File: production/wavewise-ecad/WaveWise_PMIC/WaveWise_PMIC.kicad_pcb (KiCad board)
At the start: 4 copper layers, 88.9 x 80 mm, 63 parts, among them IC1 LV14360PDDAR, J10 5031590200, J11 5031590200, J13 Screw_Terminal_01x03, J2 Conn_01x06_Pin, J3 Conn_01x03_Pin, J5 5031590400, J6 5031590400, J8 5031590800, J9 5031590300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

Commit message: Update WaveWise_PMIC.kicad_pcb
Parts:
- moved J2 1.02 mm to (59.7, 80.8)
- moved R20 0.80 mm to (52.8, 59.9)
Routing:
- net /Connectors/GPIO4: track 0.00 -> 7.37 mm
- net /Connectors/GPIO3: track 0.00 -> 7.37 mm
- net /Connectors/GPIO2: track 0.00 -> 7.37 mm
- net /Connectors/GPIO1: track 0.00 -> 7.37 mm
- net GND: track 88.3 -> 93.3 mm, vias 12 -> 14
- net Net-(H1-Pad1): track 0.00 -> 4.71 mm
- net panel_sense: track 53.7 -> 55.5 mm
- net batt_sense: track 58.6 -> 59.9 mm

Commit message: fix drc
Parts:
- moved R19 26.6 mm to (60.3, 55.2), turned to 0 degrees
- moved R16 23.5 mm to (60.3, 57.8), turned to 180 degrees
- moved HE1 1.61 mm to (54.6, 127.0)
- moved R1 1.27 mm to (111.5, 57.7)
- moved R2 1.27 mm to (109.2, 57.7)
- moved H1 1.08 mm to (54.6, 54.6)
- moved H2 1.08 mm to (135.9, 54.6)
- moved H4 0.36 mm to (135.9, 127.0)
- moved R23 0.25 mm to (135.8, 120.4)
- moved R20 0.25 mm to (52.6, 59.9)
- moved R12 0.13 mm to (60.2, 62.9)
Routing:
- net /Connectors/rockblock_TX: track 16.8 -> 44.7 mm
- net /Connectors/BICO_UART_TX: track 34.7 -> 7.54 mm
- net /Connectors/rockblock_RX: track 16.5 -> 41.7 mm
- net /Connectors/BICO_UART_RX: track 32.0 -> 7.54 mm
- net /Connectors/PANEL_SENSE_DIO: track 0.00 -> 6.00 mm
- net /Connectors/BATT_SENSE_DIO: track 0.00 -> 5.95 mm
- net /Connectors/Batt V Sense: track 92.2 -> 90.0 mm
- net +BATT: track 9.01 -> 10.5 mm
- net Net-(H1-Pad1): track 4.71 -> 5.26 mm

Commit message: power stuff
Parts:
- J5: footprint Unchecked:4pinmolex -> Connector_Molex:Molex_Micro-Fit_3.0_43650-0400_1x04_P3.00mm_Horizontal
- moved R26 21.5 mm to (91.4, 101.5), turned to 90 degrees
- moved J5 3.55 mm to (130.0, 76.1)
- moved R8 1.03 mm to (93.8, 101.3), turned to -90 degrees
- moved R25 0.40 mm to (62.9, 105.7), turned to 180 degrees
- moved R6 0.25 mm to (67.1, 113.3)
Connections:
- J13 pad 2: Net-(J13-Pin_2) -> /Inverter_Input
- J8 pad 5: air_comp_dio -> /Connectors/SICO_PUMP_CONTROL
- K1 pad 1: Net-(D2-A) -> +48V
- K1 pad 2: +48V -> Net-(D2-A)
- R25 pad 1: air_comp_dio -> /PUMP_CONTROL
- R25 pad 2: Net-(J13-Pin_2) -> /Connectors/SICO_PUMP_CONTROL
- R26 pad 1: Net-(J13-Pin_2) -> /PICO (BICO)/BICO_PUMP_CTRL
- R26 pad 2: /Inverter_Input -> /PUMP_CONTROL
- R8 pad 1: /PICO (BICO)/PUMP_CTRL -> /PUMP_CONTROL
- U1 pad 7: /PICO (BICO)/PUMP_CTRL -> /PICO (BICO)/BICO_PUMP_CTRL
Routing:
- net Net-(J13-Pin_2): track 81.4 -> 0.00 mm, vias 2 -> 0
- net /PICO (BICO)/PUMP_CTRL: track 52.8 -> 0.00 mm, vias 1 -> 0
- net /PICO (BICO)/BICO_PUMP_CTRL: track 0.00 -> 26.2 mm, vias 0 -> 1
- net /Inverter_Input: track 20.7 -> 35.6 mm
- net Net-(D2-A): track 21.1 -> 11.9 mm
- net +5V: track 38.5 -> 45.6 mm
- net Net-(Q2-B): track 4.90 -> 0.00 mm
- net /BOUT2: track 11.0 -> 6.31 mm
- net air_comp_dio: track 4.45 -> 0.00 mm
- net /Connectors/SICO_PUMP_CONTROL: track 0.00 -> 4.45 mm
- net /AOUT2: track 11.7 -> 7.28 mm
- net /PUMP_CONTROL: track 0.00 -> 4.42 mm, vias 0 -> 1
- net Net-(D1-K): track 30.3 -> 26.2 mm
- net GND: track 93.6 -> 96.2 mm, vias 14 -> 13
- net /AOUT1: track 10.4 -> 8.07 mm
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
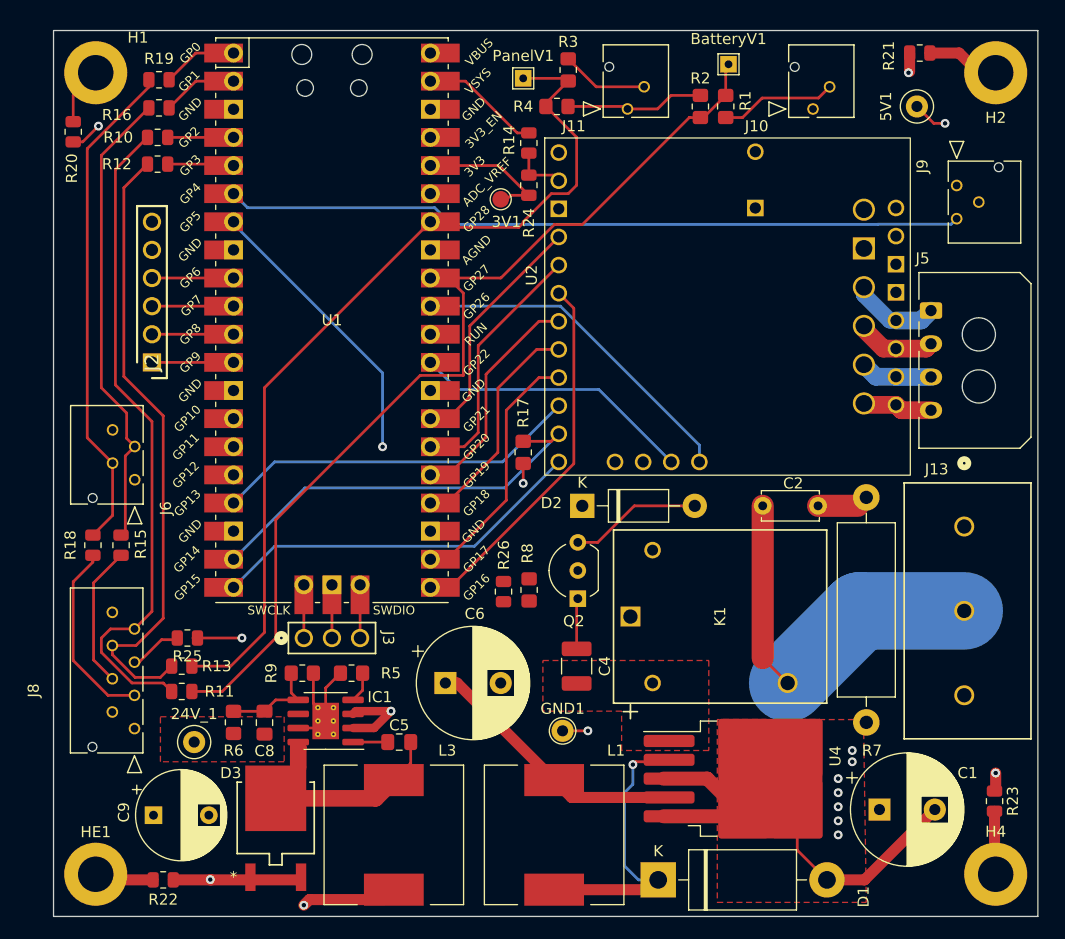
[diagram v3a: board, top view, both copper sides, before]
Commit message: add silkscreen
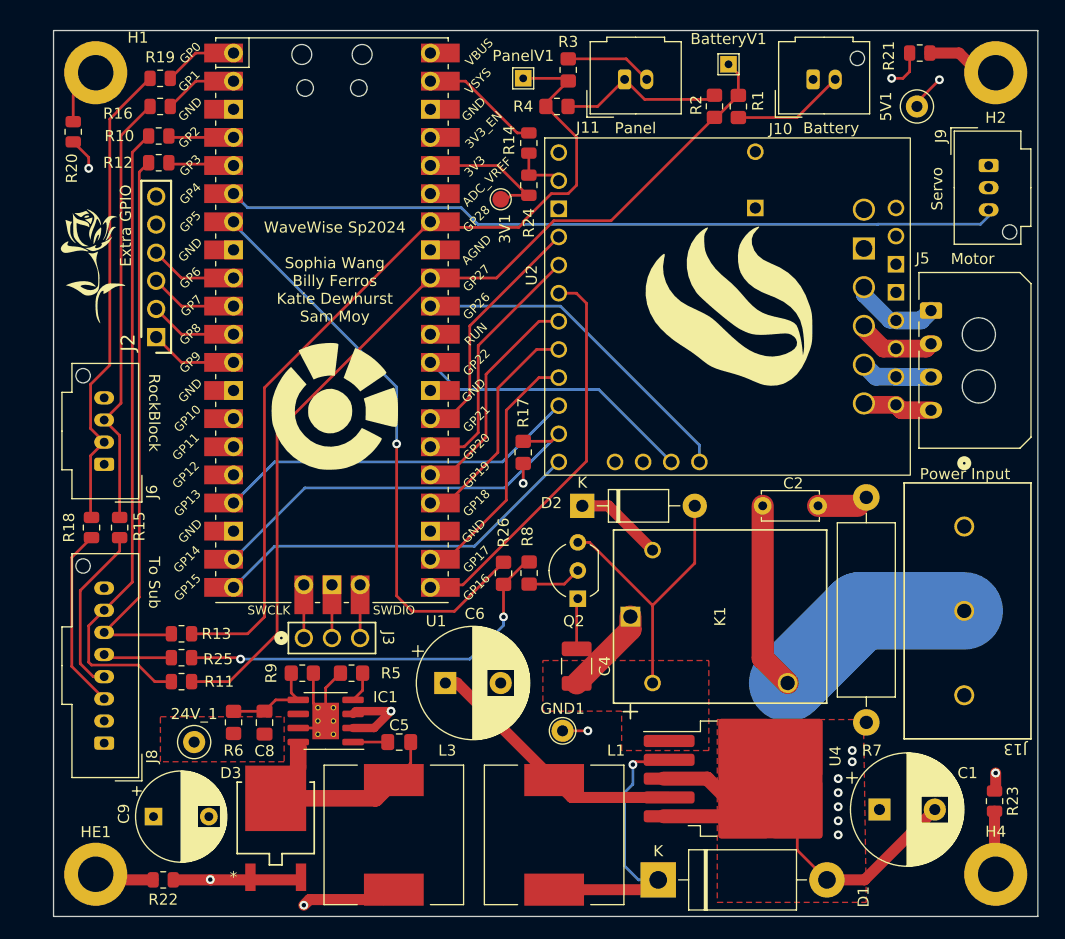
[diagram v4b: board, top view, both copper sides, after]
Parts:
- added G***: LOGO, LOGO, F.Cu at (111.8, 76.2)
- added G***: LOGO, LOGO, F.Cu at (54.4, 72.1)
- added Ge: LOGO, LOGO, F.Cu at (76.2, 85.3)
- J10: footprint Unchecked:2pinmolex -> Connector_Molex:Molex_MicroClasp_55932-0210_1x02_P2.00mm_Vertical
- J11: footprint Unchecked:2pinmolex -> Connector_Molex:Molex_MicroClasp_55932-0230_1x02_P2.00mm_Vertical
- J6: footprint Unchecked:4pinmolex -> Connector_Molex:Molex_MicroClasp_55932-0410_1x04_P2.00mm_Vertical
- J8: footprint Unchecked:8pinmolex -> Connector_Molex:Molex_MicroClasp_55932-0810_1x08_P2.00mm_Vertical
- J9: footprint Unchecked:3pinmolex -> Connector_Molex:Molex_MicroClasp_55932-0310_1x03_P2.00mm_Vertical
- R26: footprint Resistor_SMD:R_0805_2012Metric -> Resistor_SMD:R_0805_2012Metric_Pad1.20x1.40mm_HandSolder
- moved J9 3.40 mm to (135.3, 63.0)
- moved J6 3.09 mm to (55.4, 90.0)
- moved J8 3.04 mm to (55.4, 115.2)
- moved R13 2.92 mm to (62.4, 105.3)
- moved J11 2.68 mm to (102.4, 55.2)
- moved J10 2.67 mm to (119.4, 55.2)
- moved J2 2.32 mm to (60.1, 78.5)
- moved R25 1.86 mm to (62.4, 107.4)
- moved R26 1.65 mm to (91.4, 99.8), turned to -90 degrees
- moved R15 1.60 mm to (56.8, 95.7)
- moved R18 1.60 mm to (54.2, 95.7)
- moved R8 1.52 mm to (93.8, 99.8)
- moved R2 1.27 mm to (110.5, 57.6)
- moved R1 1.14 mm to (112.6, 57.7)
- moved R11 0.89 mm to (62.4, 109.6)
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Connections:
- C4 pad 2: GND -> +48V
- Q2 pad 1: GND -> +48V
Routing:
- net /PUMP_CONTROL: track 4.42 -> 36.3 mm, vias 1 -> 2
- net /PICO (BICO)/BICO_PUMP_CTRL: track 26.2 -> 51.9 mm
- net Net-(D2-A): track 11.9 -> 26.7 mm
- net +48V: track 7.59 -> 20.2 mm
- net panel_sense: track 56.6 -> 50.2 mm
- net GND: track 96.2 -> 90.0 mm
- net Net-(Q2-B): track 0.00 -> 4.91 mm
- net /Connectors/Batt V Sense: track 90.0 -> 85.6 mm
- net /Connectors/PWM_Servo: track 66.7 -> 70.2 mm
- net /Connectors/rockblock_RX: track 42.1 -> 39.4 mm
- net /Connectors/SICO_RX: track 12.9 -> 15.5 mm
- net /Connectors/rockblock_TX: track 45.1 -> 42.9 mm
- net batt_sense: track 60.1 -> 58.0 mm
- net /Connectors/Panel V Sense: track 81.7 -> 79.7 mm
- net /Connectors/SICO_PUMP_CONTROL: track 4.45 -> 6.10 mm
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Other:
- board text added: "Battery"
- board text added: "Extra GPIO"
- board text added: "Motor"
- board text added: "Panel"
- board text added: "Power Input"
- board text added: "RockBlock"
- board text added: "Servo"
- board text added: "To Sub"
- board text added: "WaveWise Sp2024 Sophia Wang Billy Ferros Katie Dewhurst Sam Moy"

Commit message: change pins on pico for layout
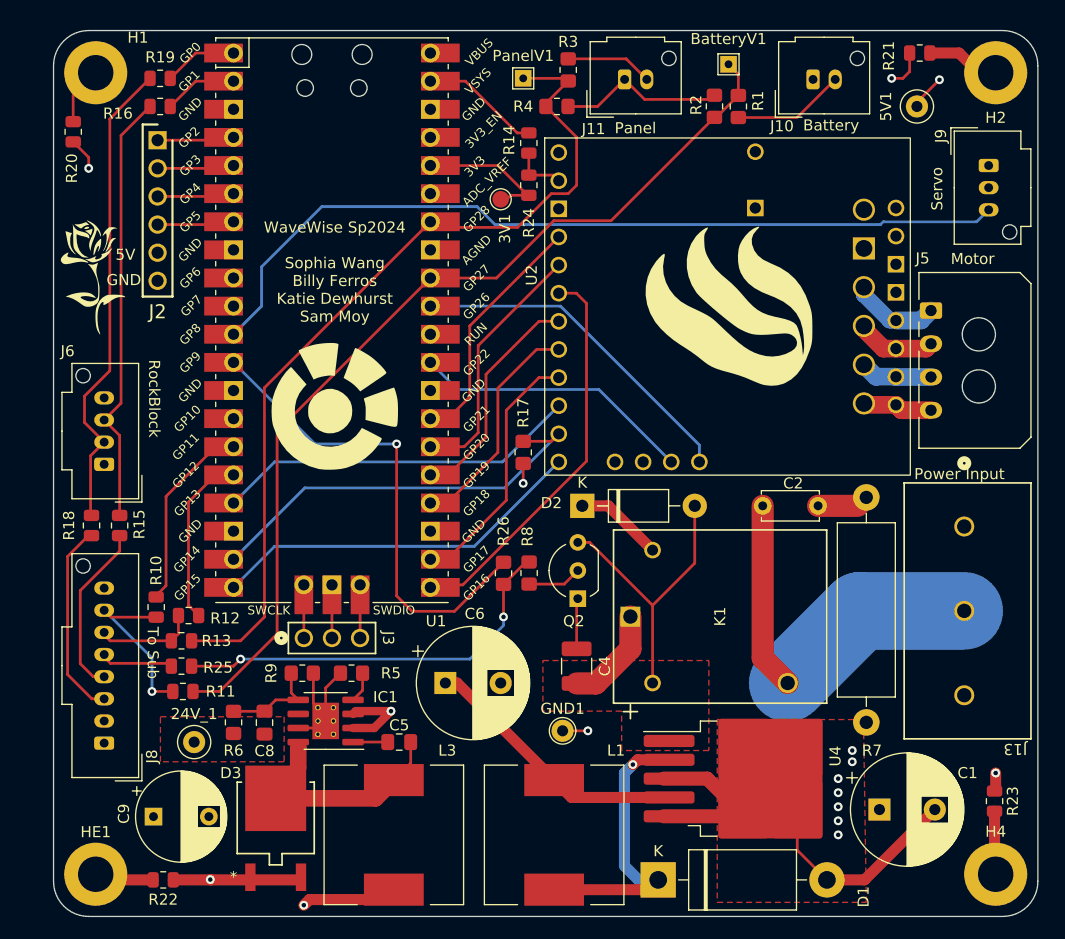
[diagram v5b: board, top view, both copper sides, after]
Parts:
- J11: footprint Connector_Molex:Molex_MicroClasp_55932-0230_1x02_P2.00mm_Vertical -> Connector_Molex:Molex_MicroClasp_55932-0210_1x02_P2.00mm_Vertical
- moved R10 42.5 mm to (60.1, 102.9), turned to 90 degrees
- moved R12 41.0 mm to (63.0, 103.6)
- moved J2 17.8 mm to (60.2, 60.7), turned to -90 degrees
- moved G1 1.02 mm to (54.4, 73.2)
- moved R11 0.90 mm to (62.5, 110.5)
- moved R25 0.76 mm to (62.4, 108.2)
- moved R13 0.64 mm to (62.4, 105.9)
- moved R15 0.18 mm to (56.8, 95.5)
- moved R18 0.18 mm to (54.2, 95.5)
- renumbered G*** to G1, G*** to G2
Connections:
- C4 pad 2: +48V -> GND
- J2 pad 1: /Connectors/GPIO4 -> /Connectors/GPIO1
- J2 pad 2: /Connectors/GPIO3 -> /Connectors/GPIO2
- J2 pad 3: /Connectors/GPIO2 -> /Connectors/GPIO3
- J2 pad 4: /Connectors/GPIO1 -> /Connectors/GPIO4
- Q2 pad 1: +48V -> GND
- U1 pad 10: /Connectors/GPIO2 -> unconnected-(U1-GPIO7-Pad10)
- U1 pad 11: /Connectors/GPIO3 -> /Connectors/PWM_Servo
- U1 pad 12: /Connectors/GPIO4 -> /PICO (BICO)/BICO_PUMP_CTRL
- U1 pad 15: unconnected-(U1-GPIO11-Pad15) -> /Connectors/BATT_SENSE_DIO
- U1 pad 16: unconnected-(U1-GPIO12-Pad16) -> /Connectors/PANEL_SENSE_DIO
- U1 pad 4: /Connectors/BATT_SENSE_DIO -> /Connectors/GPIO1
- U1 pad 5: /Connectors/PANEL_SENSE_DIO -> /Connectors/GPIO2
- U1 pad 6: /Connectors/PWM_Servo -> /Connectors/GPIO3
- U1 pad 7: /PICO (BICO)/BICO_PUMP_CTRL -> /Connectors/GPIO4
- U1 pad 9: /Connectors/GPIO1 -> unconnected-(U1-GPIO6-Pad9)
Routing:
- net batt_sense: track 58.0 -> 16.1 mm, vias 0 -> 1
- net panel_sense: track 50.2 -> 8.84 mm
- net /Connectors/BATT_SENSE_DIO: track 5.95 -> 17.5 mm
- net /Connectors/PANEL_SENSE_DIO: track 6.00 -> 15.7 mm
- net /PICO (BICO)/BICO_PUMP_CTRL: track 51.9 -> 43.6 mm
- net /Connectors/PWM_Servo: track 70.2 -> 76.3 mm
- net GND: track 90.0 -> 94.6 mm
- net +48V: track 20.2 -> 16.7 mm
- net /Connectors/SICO_TX: track 16.5 -> 17.7 mm
- net /Connectors/GPIO3: track 7.93 -> 6.96 mm
- net /Connectors/GPIO1: track 7.93 -> 6.96 mm
- net /Connectors/GPIO2: track 7.93 -> 7.14 mm
- net /Connectors/GPIO4: track 7.93 -> 7.15 mm
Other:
- outline, holes or cut-outs redrawn
- board text added: "5V"
- board text added: "GND"
- board text removed: "Extra GPIO"

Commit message: add back in 24V output
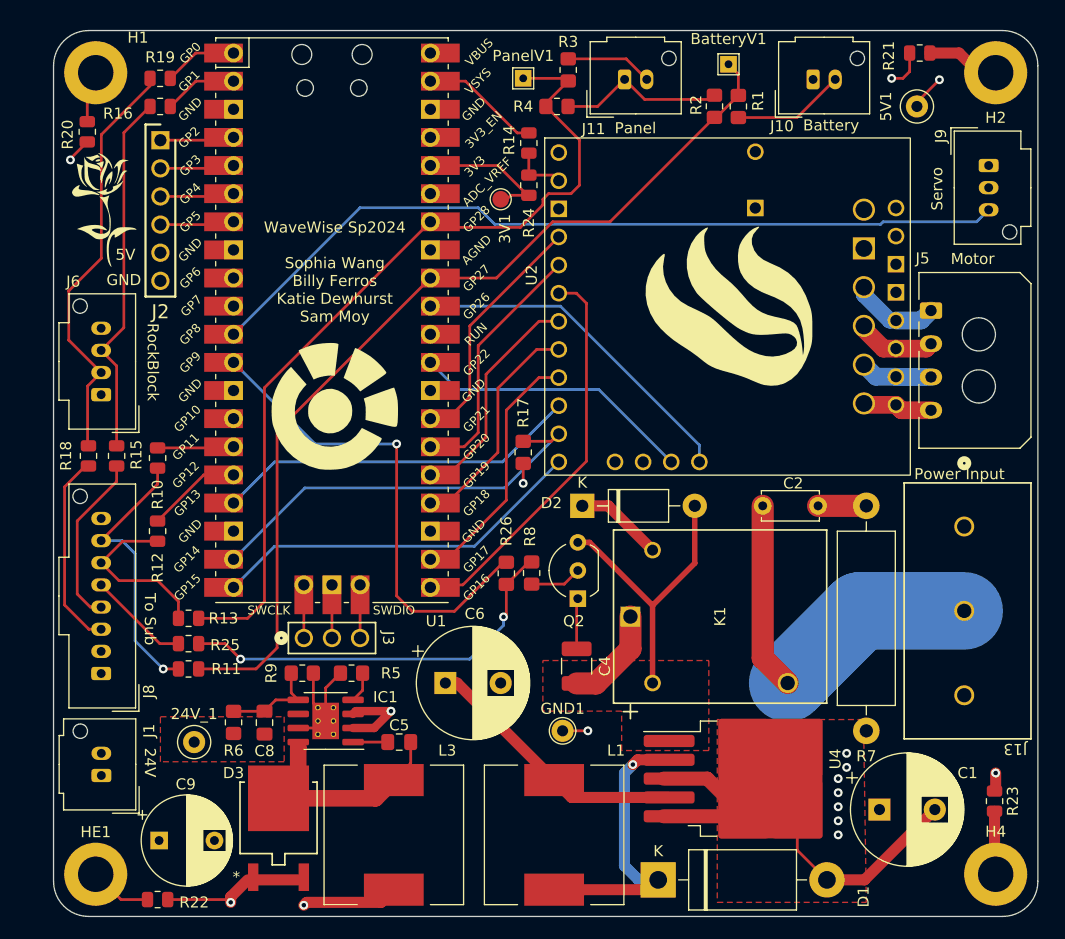
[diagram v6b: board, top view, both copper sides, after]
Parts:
- added J1: 5031590200, Connector_Molex:Molex_MicroClasp_55932-0210_1x02_P2.00mm_Vertical, F.Cu at (55.1, 118.1)
- moved R10 13.5 mm to (60.2, 89.4)
- moved R12 8.12 mm to (60.2, 96.0), turned to 90 degrees
- moved J6 6.29 mm to (55.1, 83.7)
- moved R15 6.29 mm to (56.5, 89.2)
- moved R18 6.29 mm to (54.0, 89.2)
- moved J8 6.29 mm to (55.1, 108.9)
- moved G1 6.18 mm to (55.4, 67.1)
- moved C9 2.22 mm to (60.3, 124.0)
- moved R13 2.13 mm to (63.0, 103.9)
- moved R25 2.13 mm to (63.0, 106.2)
- moved R11 2.09 mm to (63.0, 108.5)
- moved R22 1.85 mm to (60.2, 129.3)
- moved R20 1.27 mm to (53.8, 59.9)
- moved R7 0.76 mm to (124.2, 93.7)
- moved D3 0.25 mm to (71.1, 121.9)
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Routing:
- net /Connectors/BATT_SENSE_DIO: track 17.5 -> 6.90 mm
- net batt_sense: track 16.1 -> 25.3 mm
- net /Connectors/PANEL_SENSE_DIO: track 15.7 -> 8.58 mm
- net panel_sense: track 8.84 -> 15.9 mm
- net /Connectors/rockblock_RX: track 39.4 -> 33.2 mm
- net /Connectors/rockblock_TX: track 43.4 -> 38.2 mm
- net Net-(HE1-Pad1): track 5.52 -> 8.50 mm
- net /Connectors/SICO_PUMP_CONTROL: track 6.41 -> 9.18 mm
- net /Connectors/PWM_Servo: track 76.3 -> 74.1 mm
- net /Connectors/Panel V Sense: track 79.9 -> 78.3 mm
- net GND: track 94.6 -> 95.5 mm
- net /Connectors/Batt V Sense: track 85.8 -> 85.2 mm
- net Net-(H1-Pad1): track 5.26 -> 4.74 mm
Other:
- board text added: "24V"

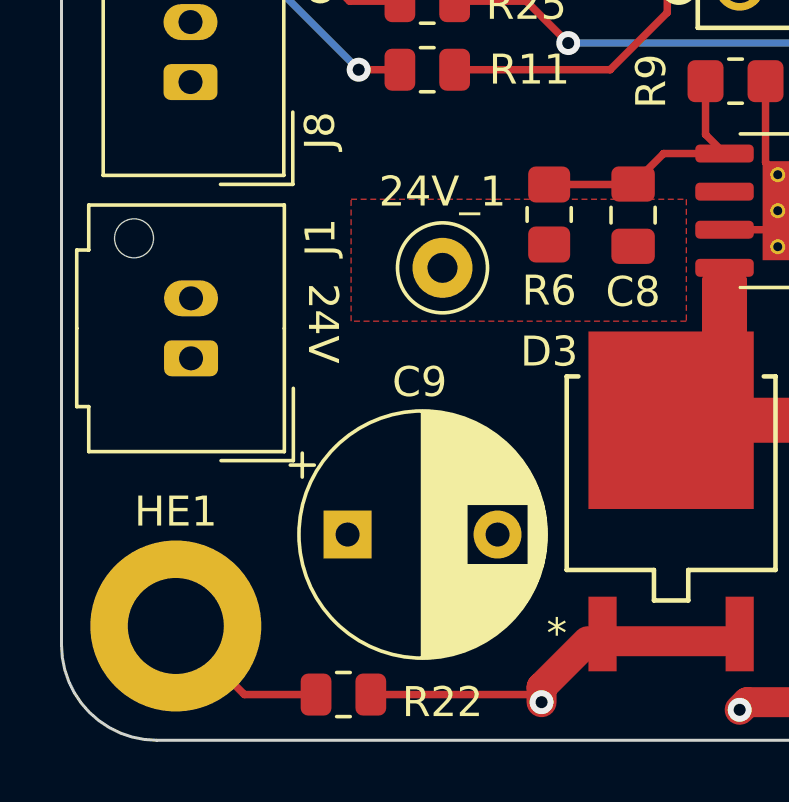
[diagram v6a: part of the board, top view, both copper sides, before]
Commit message: change 24V from microclasp to microfit
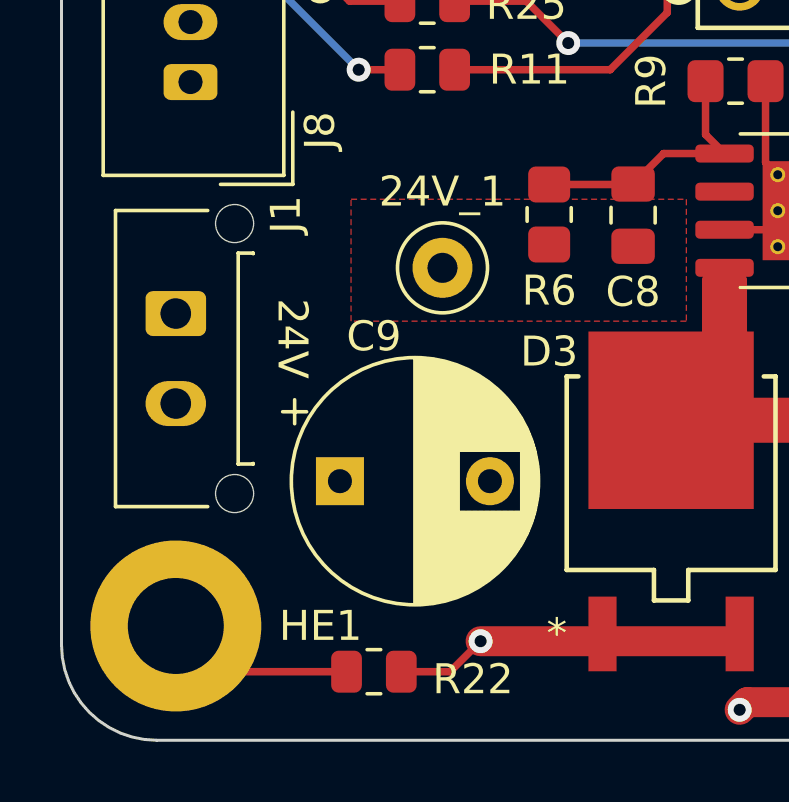
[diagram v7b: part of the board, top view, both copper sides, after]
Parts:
- J1: footprint Connector_Molex:Molex_MicroClasp_55932-0210_1x02_P2.00mm_Vertical -> Connector_Molex:Molex_Micro-Fit_3.0_43650-0215_1x02_P3.00mm_Vertical
- moved C9 1.80 mm to (60.1, 122.2)
- moved J1 1.58 mm to (54.6, 116.6), turned to -90 degrees
- moved R22 1.27 mm to (61.2, 128.5)
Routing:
- net GND: track 95.5 -> 93.7 mm
- net Net-(HE1-Pad1): track 8.50 -> 9.20 mm

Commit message: add gerber files
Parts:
- 3V1: footprint TestPoint:TestPoint_Pad_D1.5mm -> TestPoint:TestPoint_THTPad_D2.0mm_Drill1.0mm
- moved 3V1 5.11 mm to (90.7, 61.0)
- moved BatteryV1 0.25 mm to (111.8, 54.1)
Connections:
- J2 pad 5: +5V -> GND
- J2 pad 6: GND -> +5V
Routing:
- net +3.3V: track 12.7 -> 16.0 mm
- net /Connectors/Panel V Sense: track 78.3 -> 77.6 mm
- net GND: track 93.7 -> 93.1 mm
- net +48V: vias 1 -> 5
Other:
- board text added: "Extra GPIO"
- board text removed: "GND"
